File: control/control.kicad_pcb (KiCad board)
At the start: 4 copper layers, 45.7 x 39.4 mm, 85 parts, among them M1 LMR62014, M2 LM46001, M3 STM32F4XX, M4 TPS736XX, M5 SN65HVD23X, P1 PLS_2, P2 PLS_4, P3 PLS_4, P4 PLS_10, P5 PLS_3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

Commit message: Going to make a rev2.
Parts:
- moved C8 0.83 mm to (132.1, 89.7)
- moved C1 0.64 mm to (102.2, 84.5)
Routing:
- net GND: track 136.2 -> 134.5 mm
- net +5V: track 75.9 -> 76.5 mm
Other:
- board text added: "PMC rev2"
- board text removed: "PMC rev1"
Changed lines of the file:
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@@
     (thickness 1.6)
     (drawings 7)
-    (tracks 626)
+    (tracks 624)
     (zones 0)
     (modules 85)
@@
   (title_block
     (title "Phobia Control Board")
-    (date 2016-01-31)
-    (rev 1)
+    (date 2016-02-02)
+    (rev 2)
     (company "Roman Belov")
   )
@@
   )
   (setup
-    (last_trace_width 0.254)
+    (last_trace_width 0.508)
     (user_trace_width 0.381)
     (user_trace_width 0.508)
@@
     (mod_text_size 1 1)
     (mod_text_width 0.15)
-    (pad_size 1 0.25)
+    (pad_size 2.286 5.842)
     (pad_drill 0)
     (pad_to_mask_clearance 0.1)
@@
   )
   (module foot:SM0805 (layer B.Cu)
-    (at 101.6 84.455 270)
+    (at 102.235 84.455 270)
     (attr smd)
     (fp_text reference C1 (at 0 0 270) (layer B.SilkS)
@@
     (fp_line (start -2.794 2.54) (end 2.794 2.54) (layer B.SilkS) (width 0.15))
     (pad 1 smd rect (at -3.048 0 180) (size 2.286 5.842) (layers B.Cu B.Paste B.Mask)
-      (net 2 +36V))
+      (net 2 +36V) (zone_connect 2))
     (pad 2 smd rect (at 3.048 0 180) (size 2.286 5.842) (layers B.Cu B.Paste B.Mask)
       (net 78 GND) (zone_connect 2))
@@
   )
   (module foot:SM0603 (layer F.Cu)
-    (at 132.08 88.9 270)
+    (at 132.08 89.7255 270)
     (attr smd)
     (fp_text reference C8 (at 0 0 270) (layer F.SilkS)
@@
     (arrow2b (pts (xy 97.155 55.245) (xy 98.281504 54.658579)))
   )
-  (gr_text "PMC\nrev1" (at 121.92 96.52) (layer B.Cu)
+  (gr_text "PMC\nrev2" (at 121.92 96.52) (layer B.Cu)
     (effects (font (size 1.5 1.5) (thickness 0.3)) (justify mirror))
   )
@@
   (gr_line (start 142.875 60.325) (end 142.875 99.695) (layer Edge.Cuts) (width 0.15))
   (gr_line (start 97.155 60.325) (end 142.875 60.325) (layer Edge.Cuts) (width 0.15))
+  (segment (start 102.235 83.312) (end 100.457 83.312) (width 0.889) (layer B.Cu) (net 1))
+  (segment (start 100.457 83.312) (end 100.33 83.185) (width 0.889) (layer B.Cu) (net 1))
   (segment (start 113.157 78.105) (end 113.157 77.47) (width 0.508) (layer F.Cu) (net 1))
   (via (at 113.157 77.47) (size 0.7) (drill 0.3) (layers F.Cu B.Cu) (net 1))
@@
   (segment (start 111.887 74.93) (end 113.157 76.2) (width 0.508) (layer F.Cu) (net 1))
   (via (at 113.157 76.2) (size 0.7) (drill 0.3) (layers F.Cu B.Cu) (net 1))
-  (segment (start 101.6 83.312) (end 100.457 83.312) (width 0.889) (layer B.Cu) (net 1))
-  (segment (start 100.457 83.312) (end 100.33 83.185) (width 0.889) (layer B.Cu) (net 1))
   (segment (start 107.95 85.344) (end 107.823 85.344) (width 0.508) (layer F.Cu) (net 1))
   (segment (start 106.987999 86.179001) (end 106.987999 90.660201) (width 0.508) (layer F.Cu) (net 1))
@@
   (segment (start 109.22 65.151) (end 109.22 62.23) (width 1.016) (layer B.Cu) (net 2))
   (segment (start 107.188 67.183) (end 109.22 65.151) (width 1.016) (layer B.Cu) (net 2))
-  (segment (start 131.6355 85.09) (end 131.6355 86.5505) (width 0.508) (layer B.Cu) (net 3))
-  (segment (start 131.6355 86.5505) (end 132.08 86.995) (width 0.508) (layer B.Cu) (net 3))
+  (segment (start 131.0005 86.36) (end 131.0005 86.5505) (width 0.508) (layer F.Cu) (net 3))
+  (segment (start 131.0005 86.5505) (end 132.08 87.63) (width 0.508) (layer F.Cu) (net 3))
+  (segment (start 132.08 87.63) (end 132.08 88.9) (width 0.508) (layer F.Cu) (net 3))
+  (segment (start 131.6355 85.09) (end 131.6355 87.1855) (width 0.508) (layer B.Cu) (net 3))
+  (segment (start 131.6355 87.1855) (end 132.08 87.63) (width 0.508) (layer B.Cu) (net 3))
+  (via (at 132.08 87.63) (size 0.7) (drill 0.3) (layers F.Cu B.Cu) (net 3))
   (segment (start 117.0305 93.345) (end 117.0305 95.0595) (width 0.508) (layer F.Cu) (net 3))
   (segment (start 117.0305 95.0595) (end 116.84 95.25) (width 0.508) (layer F.Cu) (net 3))
@@
   (segment (start 135.89 81.0895) (end 135.4895 81.49) (width 0.254) (layer F.Cu) (net 3))
   (segment (start 135.4895 81.49) (end 133.97 81.49) (width 0.254) (layer F.Cu) (net 3))
-  (segment (start 132.08 88.0745) (end 132.08 86.995) (width 0.508) (layer F.Cu) (net 3))
-  (via (at 132.08 86.995) (size 0.7) (drill 0.3) (layers F.Cu B.Cu) (net 3))
   (segment (start 124.52 84.44) (end 124.52 84.5855) (width 0.254) (layer F.Cu) (net 3))
   (segment (start 124.52 84.5855) (end 123.3805 85.725) (width 0.254) (layer F.Cu) (net 3))
-  (segment (start 131.0005 86.36) (end 131.0005 86.995) (width 0.508) (layer F.Cu) (net 3))
-  (segment (start 131.0005 86.995) (end 132.08 88.0745) (width 0.508) (layer F.Cu) (net 3))
   (segment (start 130.52 84.44) (end 130.52 85.8795) (width 0.254) (layer F.Cu) (net 3))
   (segment (start 130.52 85.8795) (end 131.0005 86.36) (width 0.254) (layer F.Cu) (net 3))
@@
   (segment (start 138.43 94.8055) (end 140.1445 94.8055) (width 0.254) (layer B.Cu) (net 77))
   (segment (start 140.1445 94.8055) (end 140.97 93.98) (width 0.254) (layer B.Cu) (net 77))
+  (segment (start 132.08 90.551) (end 132.08 92.075) (width 0.508) (layer F.Cu) (net 78))
+  (via (at 132.08 92.075) (size 0.7) (drill 0.3) (layers F.Cu B.Cu) (net 78))
+  (segment (start 104.775 85.09) (end 105.41 85.09) (width 0.508) (layer F.Cu) (net 78))
+  (segment (start 104.14 85.09) (end 104.775 85.09) (width 0.508) (layer F.Cu) (net 78))
+  (via (at 104.775 85.09) (size 0.7) (drill 0.3) (layers F.Cu B.Cu) (net 78))
+  (segment (start 102.235 85.598) (end 100.838 85.598) (width 0.508) (layer B.Cu) (net 78))
+  (segment (start 100.838 85.598) (end 100.33 85.09) (width 0.508) (layer B.Cu) (net 78))
   (segment (start 109.728 78.105) (end 109.728 77.47) (width 0.508) (layer F.Cu) (net 78))
   (via (at 109.728 77.47) (size 0.7) (drill 0.3) (layers F.Cu B.Cu) (net 78))
@@
   (via (at 114.3 98.425) (size 0.7) (drill 0.3) (layers F.Cu B.Cu) (net 78))
   (via (at 111.125 98.425) (size 0.7) (drill 0.3) (layers F.Cu B.Cu) (net 78))
-  (segment (start 102.87 85.09) (end 104.14 85.09) (width 0.508) (layer B.Cu) (net 78))
-  (segment (start 101.6 85.598) (end 102.362 85.598) (width 0.508) (layer B.Cu) (net 78))
-  (segment (start 102.362 85.598) (end 102.87 85.09) (width 0.508) (layer B.Cu) (net 78))
-  (segment (start 101.6 85.598) (end 100.838 85.598) (width 0.508) (layer B.Cu) (net 78))
-  (segment (start 100.838 85.598) (end 100.33 85.09) (width 0.508) (layer B.Cu) (net 78))
   (segment (start 116.84 86.995) (end 117.475 86.995) (width 0.254) (layer B.Cu) (net 78))
   (via (at 117.475 86.995) (size 0.7) (drill 0.3) (layers F.Cu B.Cu) (net 78))
@@
   (segment (start 102.235 73.025) (end 102.87 72.39) (width 0.508) (layer F.Cu) (net 78))
   (via (at 102.87 72.39) (size 0.7) (drill 0.3) (layers F.Cu B.Cu) (net 78))
-  (via (at 102.87 85.09) (size 0.7) (drill 0.3) (layers F.Cu B.Cu) (net 78))
   (segment (start 122.9995 70.485) (end 121.92 70.485) (width 0.508) (layer F.Cu) (net 78))
   (via (at 121.92 70.485) (size 0.7) (drill 0.3) (layers F.Cu B.Cu) (net 78))
@@
   (via (at 120.65 85.725) (size 0.7) (drill 0.3) (layers F.Cu B.Cu) (net 78))
   (via (at 121.92 73.66) (size 0.7) (drill 0.3) (layers F.Cu B.Cu) (net 78))
-  (segment (start 132.08 89.7255) (end 132.08 90.805) (width 0.508) (layer F.Cu) (net 78))
-  (via (at 132.08 90.805) (size 0.7) (drill 0.3) (layers F.Cu B.Cu) (net 78))
   (segment (start 129.3495 86.36) (end 129.3495 86.8045) (width 0.508) (layer F.Cu) (net 78))
   (via (at 130.175 87.63) (size 0.7) (drill 0.3) (layers F.Cu B.Cu) (net 78))
@@
   (segment (start 100.7745 84.6455) (end 100.33 85.09) (width 0.508) (layer F.Cu) (net 78))
   (via (at 100.33 85.09) (size 0.7) (drill 0.3) (layers F.Cu B.Cu) (net 78))
-  (segment (start 104.14 85.09) (end 105.41 85.09) (width 0.508) (layer F.Cu) (net 78))
   (via (at 105.41 85.09) (size 0.7) (drill 0.3) (layers F.Cu B.Cu) (net 78))
   (segment (start 104.14 86.36) (end 104.14 85.09) (width 0.508) (layer F.Cu) (net 78))

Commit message: Small changes, enlarged supply rail clearance.
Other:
- net class Supply added: clearance 0.381, trace_width 0.254, via_dia 0.7, via_drill 0.3
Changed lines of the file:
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@@
   )
   (setup
-    (last_trace_width 0.508)
+    (last_trace_width 0.254)
     (user_trace_width 0.381)
     (user_trace_width 0.508)
@@
     (add_net +12V)
     (add_net +3.3V)
-    (add_net +36V)
     (add_net +5V)
     (add_net ADC_IN0)
@@
     (add_net "Net-(P6-Pad2)")
   )
+  (net_class Supply ""
+    (clearance 0.381)
+    (trace_width 0.254)
+    (via_dia 0.7)
+    (via_drill 0.3)
+    (uvia_dia 0.3)
+    (uvia_drill 0.1)
+    (add_net +36V)
+  )
   (module foot:SM1210 (layer F.Cu)

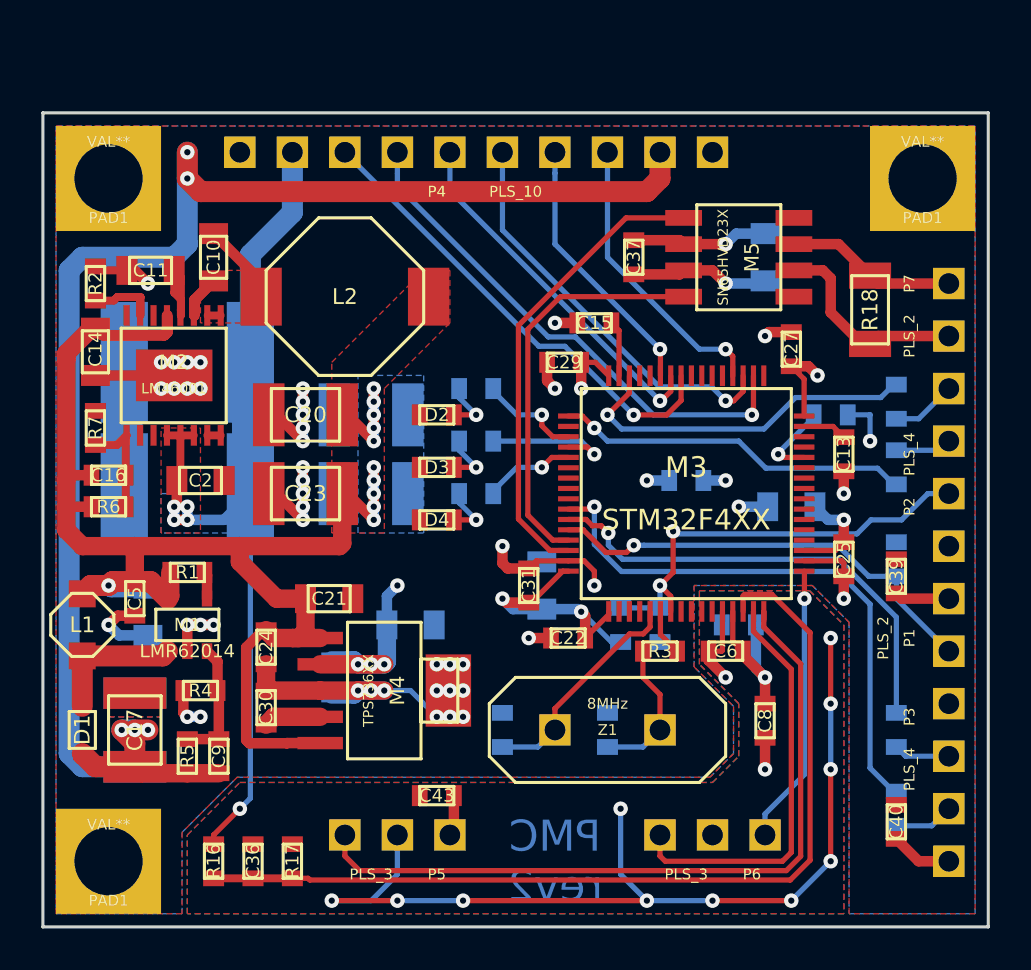
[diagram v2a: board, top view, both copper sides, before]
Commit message: Added OpAmp buffer, a lot of small fixes.
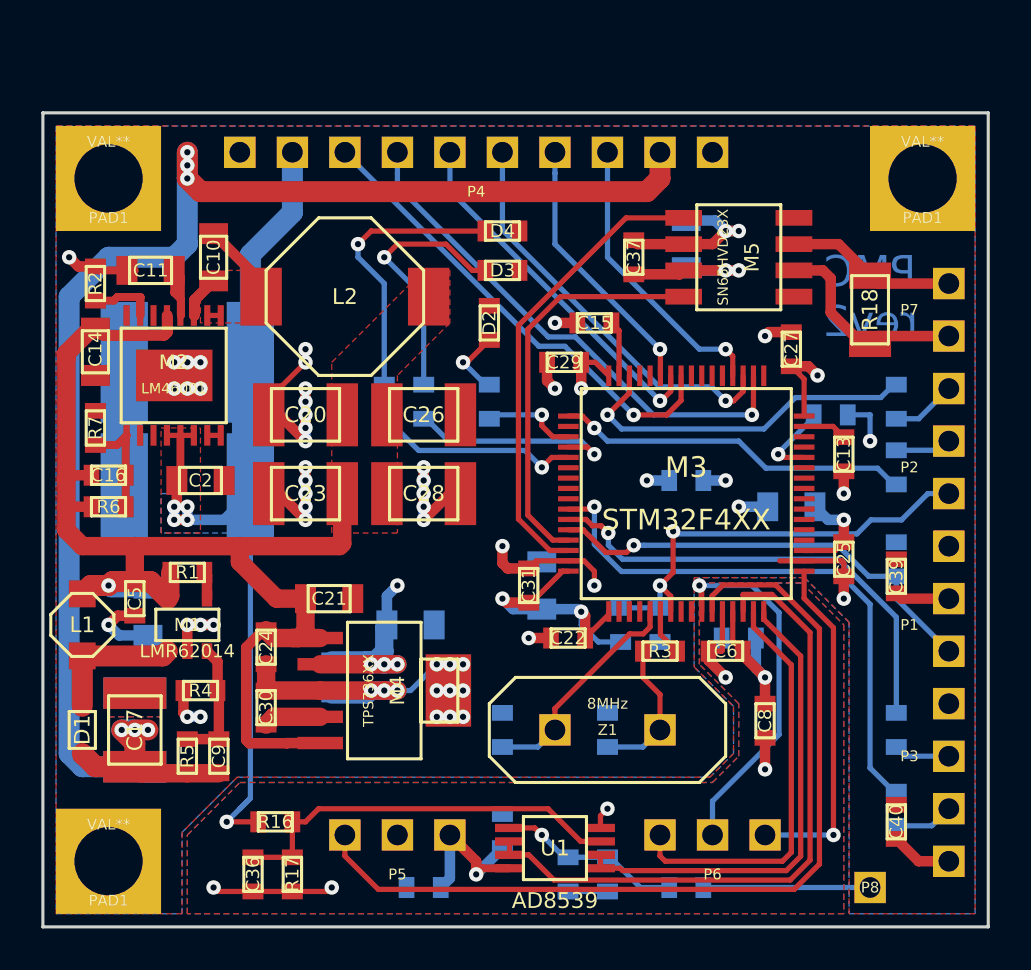
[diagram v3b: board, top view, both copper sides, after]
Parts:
- added C44: 120pF, foot:SM0603, B.Cu at (124.5, 97.2)
- added C45: 100nF, foot:SM0603, B.Cu at (119.4, 95.1)
- added P8: PLS_1, foot:PLS1, F.Cu at (137.2, 97.8)
- added R14: 470K 1%, foot:SM0603, B.Cu at (128.3, 97.8)
- added R15: 27K 1%, foot:SM0603, B.Cu at (122.6, 97.2)
- added U1: AD8539, foot:MSOP8, F.Cu at (121.9, 95.9)
- C26, C28: moved to F.Cu
- C36: value 1nF -> 120pF
- C43: moved to B.Cu
- R16: value 47K 1% -> 470K 1%
- R17: value 2K7 1% -> 27K 1%
- moved D4 14.3 mm to (119.4, 66.0), turned to 180 degrees
- moved D3 10.0 mm to (119.4, 67.9), turned to 180 degrees
- moved R21 6.29 mm to (113.7, 74.3), turned to 90 degrees
- moved D2 5.12 mm to (118.7, 70.5), turned to 270 degrees
- moved C43 4.49 mm to (115.6, 97.8)
- moved C38 3.86 mm to (128.3, 66.7)
- moved R16 3.54 mm to (108.4, 94.6), turned to 0 degrees
- moved R20 3.18 mm to (115.6, 74.3), turned to 90 degrees
- moved C26 2.54 mm to (115.6, 74.9), turned to 0 degrees
- moved C28 2.54 mm to (115.6, 78.7), turned to 0 degrees
- moved R19 0.90 mm to (118.7, 74.3), turned to 90 degrees
- moved C36 0.64 mm to (107.3, 97.2), turned to 270 degrees
- moved R17 0.64 mm to (109.2, 97.2), turned to 90 degrees
- moved C42 0.63 mm to (130.8, 85.7)
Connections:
- C36 pad 1: ADC_IN0 -> Net-(C36-Pad1)
- M3 pad 10: Net-(M3-Pad10) -> ADC_IN12
- M3 pad 11: Net-(M3-Pad11) -> ADC_IN13
- P5 pad 1: ADC_IN2 -> ADC_IN13
- P6 pad 2: Net-(P6-Pad2) -> ADC_IN12
- R16 pad 2: ADC_IN0 -> Net-(C36-Pad1)
- R17 pad 2: ADC_IN0 -> Net-(C36-Pad1)
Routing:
- net ADC_IN13: track 0.00 -> 43.6 mm
- net GND: track 134.5 -> 108.5 mm, vias 62 -> 60
- net Net-(C36-Pad1): track 0.00 -> 19.4 mm
- net ADC_IN12: track 0.00 -> 17.8 mm, vias 0 -> 1
- net ADC_IN2: track 36.6 -> 23.2 mm
- net ADC_IN0: track 45.1 -> 31.9 mm
- net Net-(D4-Pad2): track 2.69 -> 13.7 mm
- net +3.3V: track 58.5 -> 68.5 mm, vias 12 -> 14
- net Net-(D3-Pad2): track 2.69 -> 12.6 mm
- net Net-(C44-Pad1): track 0.00 -> 8.92 mm, vias 0 -> 1
- net +5V: track 76.5 -> 67.8 mm, vias 11 -> 1
- net HVIN: track 0.00 -> 8.06 mm
- net LED_BLUE: track 4.43 -> 10.1 mm
- net LED_GREEN: track 6.55 -> 10.4 mm
- net ADC_IN3: track 13.6 -> 16.7 mm
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- removed copper zone on B.Cu, net +5V

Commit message: Added encoder inputs on control board, removed SWD, changed USART.
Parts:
- removed P8: PLS_1, foot:PLS1
- removed R10, R12, R13, R9: 47, foot:SM0603
- P2: value PLS_4 -> PLS_2; footprint foot:PLS4 -> foot:PLS2
- P3: value PLS_4 -> PLS_8; footprint foot:PLS4 -> foot:PLS8
- moved P1 24.1 mm to (133.3, 62.2), turned to 180 degrees
- moved P2 19.7 mm to (139.7, 97.2), turned to 0 degrees
- moved C40 14.6 mm to (138.4, 80.0)
- moved R11 12.7 mm to (125.7, 81.3), turned to 90 degrees
- moved P3 10.2 mm to (141.0, 82.5), turned to 270 degrees
- moved C39 4.89 mm to (138.4, 87.6), turned to 270 degrees
- moved C33 0.63 mm to (128.3, 78.7), turned to 0 degrees
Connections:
- M3 pad 37: Net-(M3-Pad37) -> EN_A
- M3 pad 38: Net-(M3-Pad38) -> EN_B
- M3 pad 51: LED_RED -> USART_TX
- M3 pad 52: LED_GREEN -> USART_RX
- M3 pad 53: LED_BLUE -> Net-(M3-Pad53)
- M3 pad 55: Net-(M3-Pad55) -> LED_RED
- M3 pad 56: Net-(M3-Pad56) -> LED_GREEN
- M3 pad 57: Net-(M3-Pad57) -> LED_BLUE
- M3 pad 60: Net-(M3-Pad60) -> BOOT
- P1 pad 1: Net-(M3-Pad60) -> EN_A
- P1 pad 2: +3.3V -> EN_B
- P2 pad 1: Net-(P2-Pad1) -> HVIN
- P2 pad 2: Net-(P2-Pad2) -> GND
- P3 pad 1: +3.3V -> GND
- P3 pad 2: Net-(P3-Pad2) -> USART_TX
- P3 pad 3: Net-(P3-Pad3) -> USART_RX
- P3 pad 4: GND -> +3.3V
- R11 pad 2: Net-(M3-Pad60) -> BOOT
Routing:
- net Net-(M3-Pad58): track 27.3 -> 0.00 mm, vias 1 -> 0
- net GND: track 108.5 -> 131.6 mm, vias 60 -> 64
- net Net-(M3-Pad59): track 22.8 -> 0.00 mm, vias 1 -> 0
- net Net-(M3-Pad60): track 21.8 -> 0.00 mm, vias 1 -> 0
- net BOOT: track 0.00 -> 20.1 mm, vias 0 -> 1
- net USART_TX: track 0.00 -> 19.4 mm, vias 0 -> 1
- net USART_RX: track 0.00 -> 19.3 mm, vias 0 -> 1
- net Net-(M3-Pad46): track 17.5 -> 0.00 mm, vias 1 -> 0
- net Net-(M3-Pad49): track 17.2 -> 0.00 mm, vias 1 -> 0
- net EN_A: track 0.00 -> 12.7 mm
- net EN_B: track 0.00 -> 11.9 mm
- net Net-(P2-Pad1): track 3.41 -> 0.00 mm
- net Net-(P3-Pad2): track 2.88 -> 0.00 mm
- net Net-(P3-Pad3): track 2.72 -> 0.00 mm
- net Net-(P2-Pad2): track 2.72 -> 0.00 mm
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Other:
- board text added: "rev2"
- board text removed: "PMC rev2"

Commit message: Added DAC outputs, SWD outputs, fixes.
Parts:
- added P8: SWD, foot:PLS2, F.Cu at (138.4, 74.9)
- added R10: 10K, foot:SM0603, B.Cu at (132.6, 65.4)
- added R9: 10K, foot:SM0603, B.Cu at (134.4, 65.4)
- C39: moved to B.Cu
- P1: value PLS_2 -> ENCODER
- P2: value PLS_2 -> VOLTAGE
- P3: value PLS_8 -> CONTROL
- P4: value PLS_10 -> POWER
- P5, P6: value PLS_3 -> SENSOR
- P7: value PLS_2 -> CAN
- moved C39 7.62 mm to (138.4, 80.0), turned to 90 degrees
- moved C34 0.64 mm to (133.3, 78.7)
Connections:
- M3 pad 20: Net-(M3-Pad20) -> DAC_OUT1
- M3 pad 21: Net-(M3-Pad21) -> DAC_OUT2
- P3 pad 5: BOOT -> DAC_OUT2
- P3 pad 6: +3.3V -> DAC_OUT1
- P3 pad 7: NRST -> BOOT
- P3 pad 8: GND -> NRST
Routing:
- net Net-(M3-Pad49): track 0.00 -> 19.4 mm, vias 0 -> 1
- net Net-(M3-Pad46): track 0.00 -> 17.5 mm, vias 0 -> 1
- net DAC_OUT2: track 0.00 -> 12.2 mm, vias 0 -> 1
- net DAC_OUT1: track 0.00 -> 11.7 mm, vias 0 -> 1
- net GND: track 131.6 -> 143.1 mm, vias 64 -> 65
- net BOOT: track 20.1 -> 23.8 mm
- net EN_B: track 11.9 -> 14.4 mm
- net EN_A: track 12.7 -> 15.2 mm
- net NRST: track 23.1 -> 25.2 mm
- net +3.3V: track 69.5 -> 71.3 mm
- net +5V: track 67.8 -> 67.3 mm

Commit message: Added jumper outputs.
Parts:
- added P9: JUMPER, foot:PLS2, F.Cu at (138.4, 90.2)
- C39: moved to F.Cu
- moved C40 5.52 mm to (138.4, 85.5)
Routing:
- net GND: track 143.1 -> 133.8 mm, vias 65 -> 64
- net +3.3V: track 71.3 -> 73.8 mm
- net DAC_OUT2: track 12.2 -> 14.0 mm
- net NRST: track 25.2 -> 24.6 mm
- net BOOT: track 23.8 -> 23.2 mm
